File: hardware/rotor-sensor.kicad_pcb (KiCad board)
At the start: 2 copper layers, 30.7 x 16 mm, 33 parts, among them J1 Conn_01x03, J2 Conn_01x03, J3 Conn_01x03, U1 ATtiny202-SS, U2 EE-SX199, U3 SM351LT

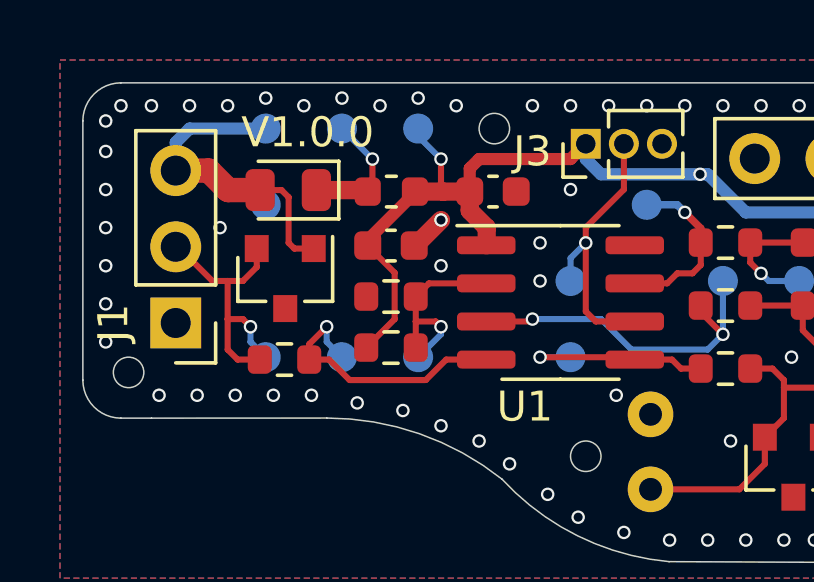
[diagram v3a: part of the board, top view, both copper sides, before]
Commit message: Rotated input filter capacitor for better ground connection
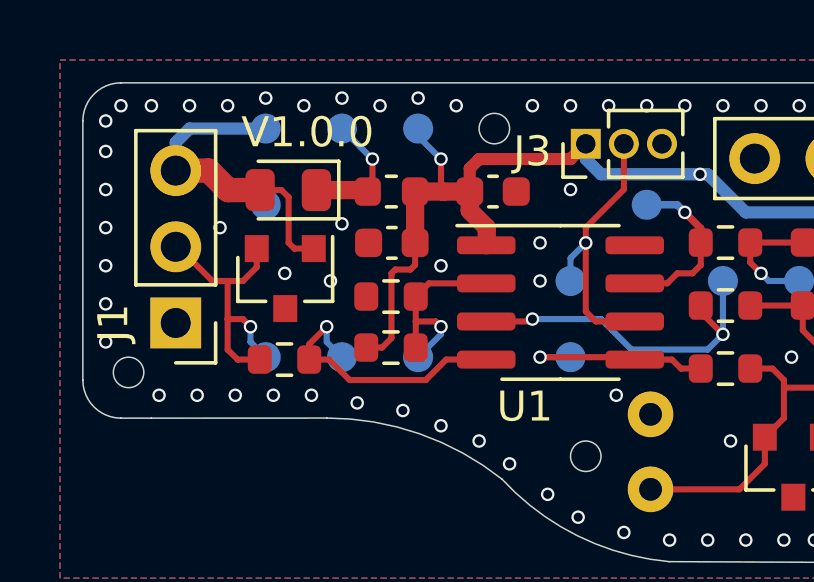
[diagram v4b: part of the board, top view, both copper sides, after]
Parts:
- moved C1 0.09 mm to (-7.90, -3.89), turned to 180 degrees
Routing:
- net GND: track 1.24 -> 0.00 mm, vias 76 -> 78
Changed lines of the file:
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@@
     (thickness 1.6)
     (drawings 17)
-    (tracks 255)
+    (tracks 258)
     (zones 0)
     (modules 33)
@@
   )
   (setup
-    (last_trace_width 0.4064)
+    (last_trace_width 0.2032)
     (user_trace_width 0.2032)
     (user_trace_width 0.4064)
@@
   )
   (module Capacitor_SMD:C_0603_1608Metric (layer F.Cu)
-    (at -7.925 -3.8)
+    (at -7.896 -3.89 180)
     (descr "Capacitor SMD 0603 (1608 Metric), square (rectangular) end terminal, IPC_7351 nominal, (Body size source: IPC-SM-782 page 76, https://www.pcb-3d.com/wordpress/wp-content/uploads/ipc-sm-782a_amendment_1_and_2.pdf), generated with kicad-footprint-generator")
     (tags capacitor)
@@
       (effects (font (size 0.4 0.4) (thickness 0.06)))
     )
-    (pad 2 smd roundrect (at 0.775 0) (size 0.9 0.95) (layers F.Cu F.Paste F.Mask) (roundrect_rratio 0.25)
-      (net 1 GND))
-    (pad 1 smd roundrect (at -0.775 0) (size 0.9 0.95) (layers F.Cu F.Paste F.Mask) (roundrect_rratio 0.25)
+    (pad 2 smd roundrect (at 0.775 0 180) (size 0.9 0.95) (layers F.Cu F.Paste F.Mask) (roundrect_rratio 0.25)
+      (net 1 GND))
+    (pad 1 smd roundrect (at -0.775 0 180) (size 0.9 0.95) (layers F.Cu F.Paste F.Mask) (roundrect_rratio 0.25)
       (net 2 +5V))
     (model ${KISYS3DMOD}/Capacitor_SMD.3dshapes/C_0603_1608Metric.wrl
@@
   (gr_arc (start -16.926 0.682) (end -18.196 0.682) (angle -90) (layer Edge.Cuts) (width 0.05))
   (gr_line (start -10.068 1.948568) (end -15.91 1.952) (layer Edge.Cuts) (width 0.05))
-  (via (at -6.258 -4.652) (size 0.45) (drill 0.3) (layers F.Cu B.Cu) (net 1))
   (via (at -6.258 -3.128) (size 0.45) (drill 0.3) (layers F.Cu B.Cu) (net 1))
   (via (at -2.956 -3.89) (size 0.45) (drill 0.3) (layers F.Cu B.Cu) (net 1))
@@
   (via (at 9.744 -0.08) (size 0.45) (drill 0.3) (layers F.Cu B.Cu) (net 1))
   (via (at 5.426 -0.08) (size 0.45) (drill 0.3) (layers F.Cu B.Cu) (net 1))
-  (segment (start -7.11 -3.8) (end -6.258 -4.652) (width 0.6096) (layer F.Cu) (net 1))
-  (segment (start -7.15 -3.8) (end -7.11 -3.8) (width 0.6096) (layer F.Cu) (net 1))
+  (segment (start -7.15 -3.8) (end -7.11 -3.8) (width 0.6096) (layer F.Cu) (net 2))
   (via (at 11.776 4.111) (size 0.45) (drill 0.3) (layers F.Cu B.Cu) (net 1))
   (via (at 11.649 5.254) (size 0.45) (drill 0.3) (layers F.Cu B.Cu) (net 1))
   (via (at 11.014 5.889) (size 0.45) (drill 0.3) (layers F.Cu B.Cu) (net 1))
   (via (at 6.188 6.016) (size 0.45) (drill 0.3) (layers F.Cu B.Cu) (net 1))
-  (segment (start -7.125 -5.6) (end -7.125 -5.563) (width 0.4064) (layer F.Cu) (net 2))
-  (segment (start -8.7 -3.988) (end -8.7 -3.8) (width 0.4064) (layer F.Cu) (net 2))
-  (segment (start -7.125 -5.563) (end -8.7 -3.988) (width 0.4064) (layer F.Cu) (net 2))
+  (via (at -9.56 -4.525) (size 0.45) (drill 0.3) (layers F.Cu B.Cu) (net 1))
+  (via (at -9.941 -2.62) (size 0.45) (drill 0.3) (layers F.Cu B.Cu) (net 1))
+  (via (at -11.465 -2.874) (size 0.45) (drill 0.3) (layers F.Cu B.Cu) (net 1))
   (via (at -6.258 -6.684) (size 0.45) (drill 0.3) (layers F.Cu B.Cu) (net 2))
   (segment (start -7.02 -7.446) (end -6.258 -6.684) (width 0.2032) (layer B.Cu) (net 2))
@@
   (segment (start -6.19 -5.6) (end -5.3 -5.6) (width 0.6096) (layer F.Cu) (net 2))
   (segment (start -7.125 -5.6) (end -6.19 -5.6) (width 0.6096) (layer F.Cu) (net 2))
-  (segment (start -7.80161 -1.34839) (end -8.75 -0.4) (width 0.2032) (layer F.Cu) (net 2))
-  (segment (start -7.80161 -2.89361) (end -7.80161 -1.34839) (width 0.2032) (layer F.Cu) (net 2))
-  (segment (start -8.7 -3.792) (end -7.80161 -2.89361) (width 0.2032) (layer F.Cu) (net 2))
-  (segment (start -8.7 -3.8) (end -8.7 -3.792) (width 0.2032) (layer F.Cu) (net 2))
   (segment (start -4.734 -3.826) (end -4.75 -3.81) (width 0.6096) (layer F.Cu) (net 2))
   (segment (start -4.734 -4.398) (end -4.734 -3.826) (width 0.6096) (layer F.Cu) (net 2))
@@
   (segment (start 7.204 0.936) (end 7.204 -0.588) (width 0.4064) (layer B.Cu) (net 2))
   (segment (start 6.442 1.698) (end 7.204 0.936) (width 0.4064) (layer B.Cu) (net 2))
+  (segment (start -7.121 -5.596) (end -7.125 -5.6) (width 0.6096) (layer F.Cu) (net 2))
+  (segment (start -7.121 -3.89) (end -7.121 -5.596) (width 0.6096) (layer F.Cu) (net 2))
+  (segment (start -7.121 -3.89) (end -7.121 -3.154) (width 0.2032) (layer F.Cu) (net 2))
+  (segment (start -7.121 -3.154) (end -7.274 -3.001) (width 0.2032) (layer F.Cu) (net 2))
+  (segment (start -7.274 -3.001) (end -7.782 -3.001) (width 0.2032) (layer F.Cu) (net 2))
+  (segment (start -7.782 -3.001) (end -7.909 -2.874) (width 0.2032) (layer F.Cu) (net 2))
+  (segment (start -7.909 -2.874) (end -7.909 -0.715) (width 0.2032) (layer F.Cu) (net 2))
+  (segment (start -8.224 -0.4) (end -8.75 -0.4) (width 0.2032) (layer F.Cu) (net 2))
+  (segment (start -7.909 -0.715) (end -8.224 -0.4) (width 0.2032) (layer F.Cu) (net 2))
   (segment (start -13.878 -2.62) (end -13.37 -2.62) (width 0.2032) (layer F.Cu) (net 3))
   (segment (start -15.018 -3.76) (end -13.878 -2.62) (width 0.2032) (layer F.Cu) (net 3))

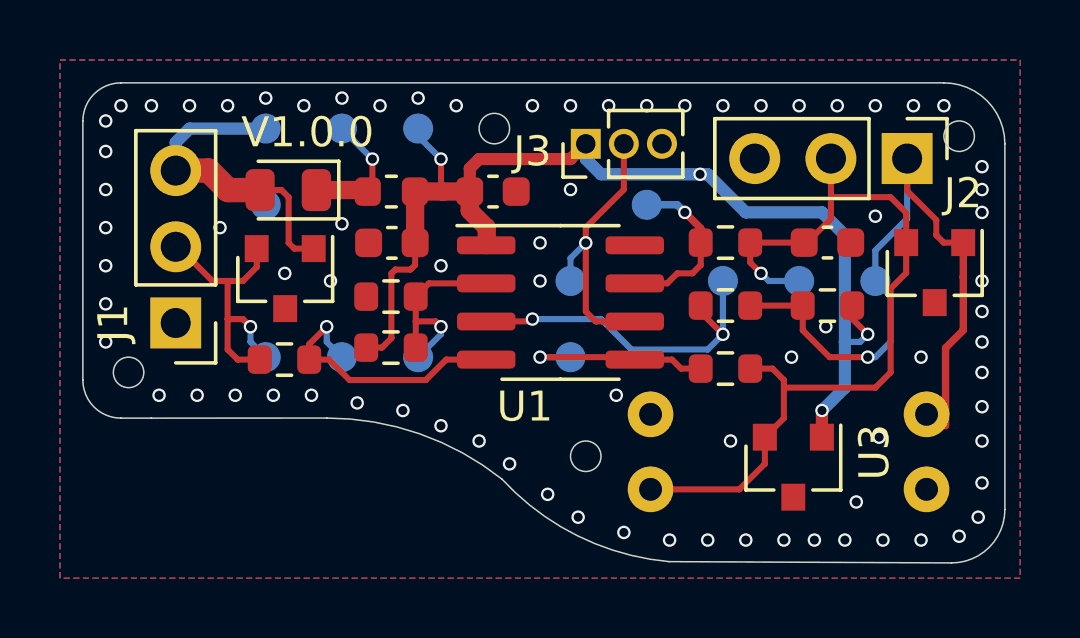
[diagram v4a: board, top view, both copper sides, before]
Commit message: Panelization workflow updates
Adds fiducials to board and added tab annotation as a footprint.
Panel configuration has been updated.
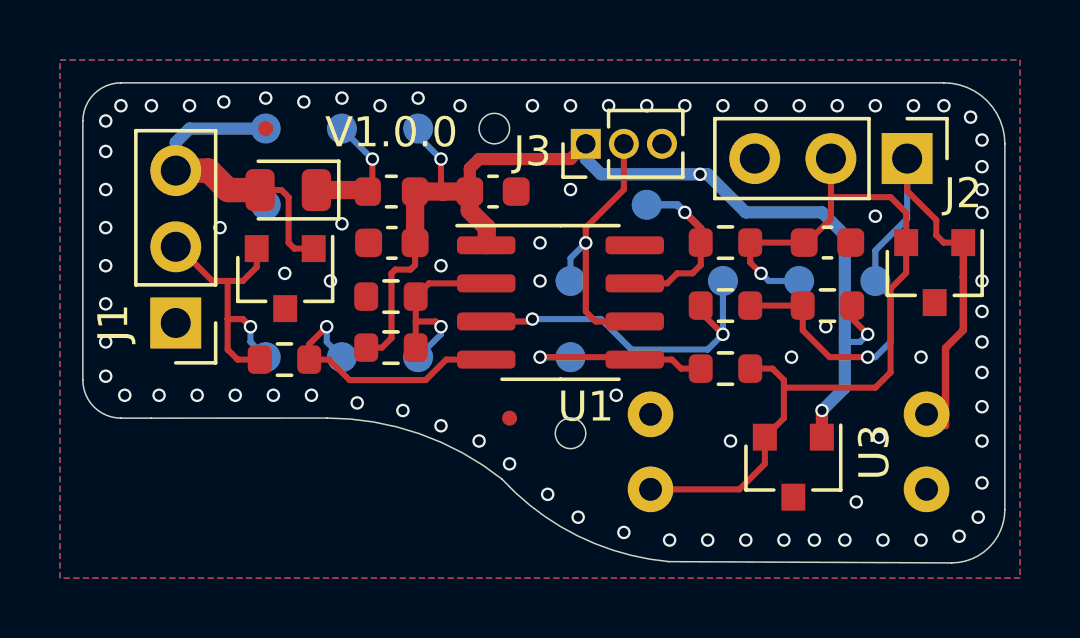
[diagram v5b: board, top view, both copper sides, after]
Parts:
- added FID1: Fiducial, Fiducial:Fiducial_0.5mm_Mask1.5mm, F.Cu at (-3.97, 1.95)
- added FID2: Fiducial, Fiducial:Fiducial_0.5mm_Mask1.5mm, F.Cu at (-12.1, -7.70)
- added REF**: Tab, local:Tab, F.Cu at (5.30, 7.29)
- added REF**: Tab, local:Tab, F.Cu at (-12.7, 2.59)
- added REF**: Tab, local:Tab, F.Cu at (6.70, -9.73)
- added REF**: Tab, local:Tab, F.Cu at (-8.93, -9.73)
- added REF**: Tab, local:Tab, F.Cu at (13.0, 1.32)
- added REF**: Tab, local:Tab, F.Cu at (-18.8, -3.38)
- C1, C2, C3: value C -> 100n
- L1: value L -> 10uH
- R1, R4, R5: value R -> 50m
- R2, R6, R7: value R -> 1k
- R3: value R -> 100
- TP2: value COM -> COMA
- TP7: value COM -> COMB
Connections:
- net Net-(D1-Pad1) renamed /Vin
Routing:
- net GND: vias 78 -> 82
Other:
- outline, holes or cut-outs redrawn

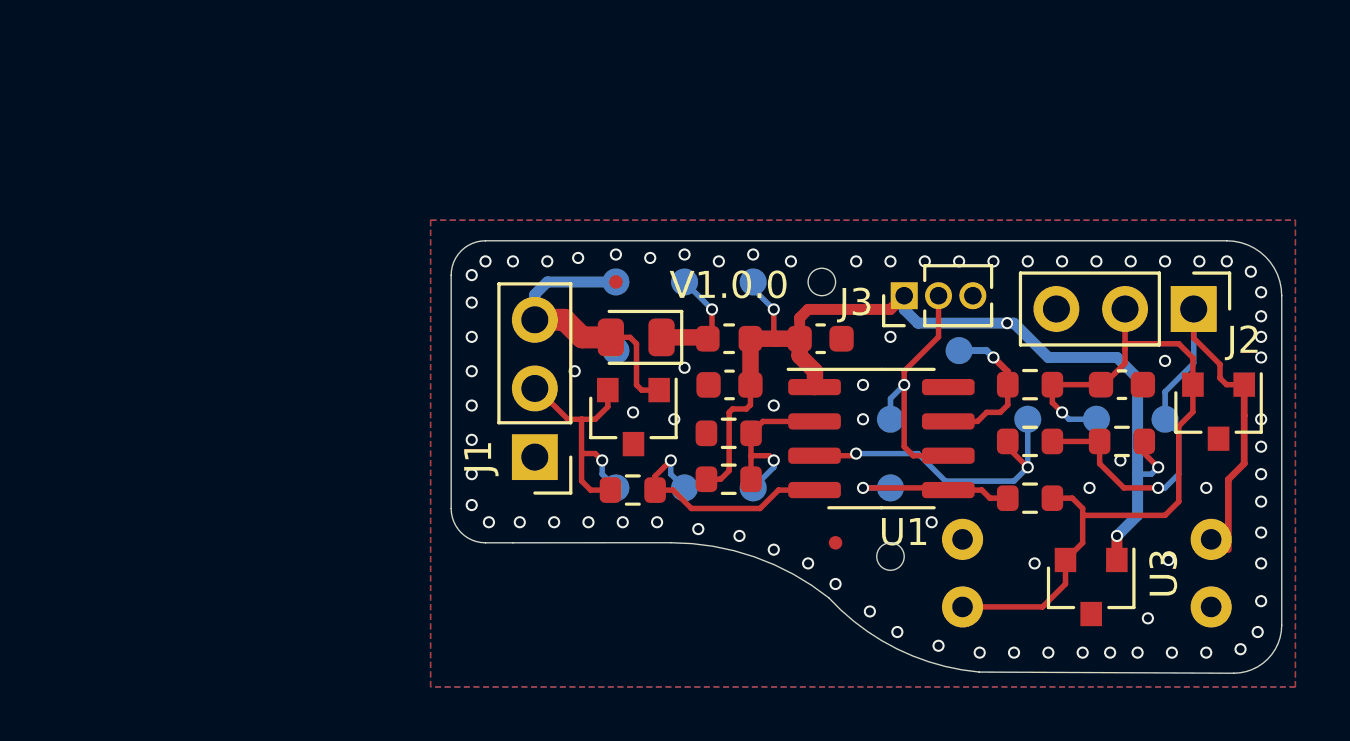
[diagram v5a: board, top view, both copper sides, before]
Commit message: Adds LIN Transceiver to the design (#7)
Updates layout and schematic, replaced test point labels on schematic
Adds overcurrent protection IC and removes sense line

Hardware container version downgrade, KiKit downgrade
Hardware workflow retention day set to 5 days and
STEP generation step is skipped due to errors

Fixes track clearance issue on panelized layout
Tight frame and 1x4 panel layout
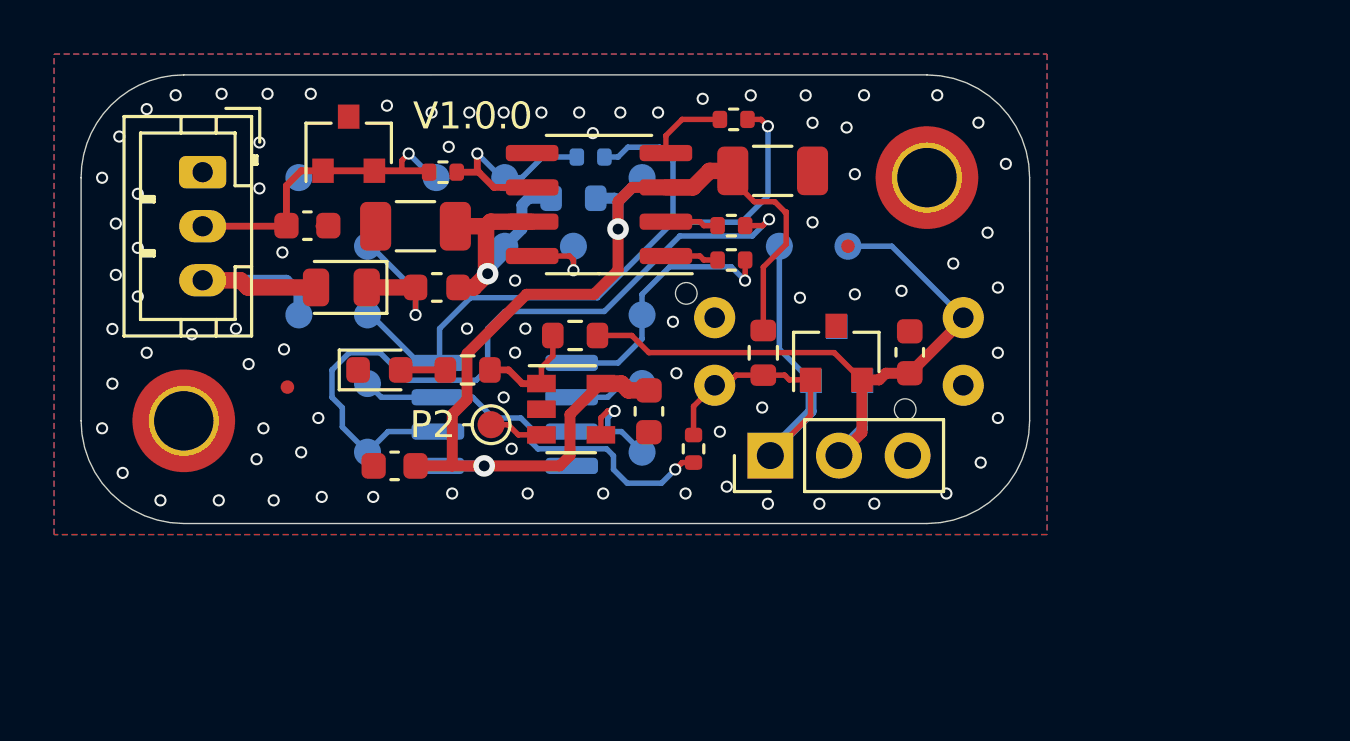
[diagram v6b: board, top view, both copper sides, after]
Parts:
- removed J3: Conn_01x03, Connector_PinHeader_1.27mm:PinHeader_1x03_P1.27mm_Vertical
- removed the R5 at (3.23, -1.80)
- removed the R6 at (-7.92, -0.40)
- removed REF** (x6): Tab, local:Tab
- added C2: 10u, Capacitor_SMD:C_1206_3216Metric, F.Cu at (-6.30, -11.8)
- added C3: 22p, Capacitor_SMD:C_0603_1608Metric, F.Cu at (-23.5, -9.78)
- added C5: 100n, Capacitor_SMD:C_0603_1608Metric, F.Cu at (-10.9, -2.91)
- added D4: LED_Small, LED_SMD:LED_0603_1608Metric, F.Cu at (-20.9, -4.45)
- added H1: MountingHole_Pad, MountingHole:MountingHole_2.2mm_M2_DIN965_Pad_TopOnly, F.Cu at (-28.1, -2.56)
- added H2: MountingHole_Pad, MountingHole:MountingHole_2.2mm_M2_DIN965_Pad_TopOnly, F.Cu at (-0.59, -11.6)
- added R1: 0, Resistor_SMD:R_0402_1005Metric, B.Cu at (-13.0, -12.3)
- added R10: 220, Resistor_SMD:R_0603_1608Metric, F.Cu at (-17.6, -4.45)
- added R2: 0, Resistor_SMD:R_0402_1005Metric, F.Cu at (-7.83, -8.51)
- added R3: 0, Resistor_SMD:R_0402_1005Metric, F.Cu at (-7.74, -13.7)
- added R9: 0, Resistor_SMD:R_0603_1608Metric, B.Cu at (-13.7, -10.8)
- added TP17: P2, TestPoint:TestPoint_Pad_D1.0mm, F.Cu at (-16.7, -2.42)
- added TP4: V3, TestPoint:TestPoint_Pad_D1.0mm, B.Cu at (-11.1, -11.6)
- added TP7: C1, TestPoint:TestPoint_Pad_D1.0mm, B.Cu at (-16.2, -11.6)
- added TP8: C2, TestPoint:TestPoint_Pad_D1.0mm, B.Cu at (-13.7, -9.02)
- added U2: MCP2021A-xxxxSN, Package_SO:SOIC-8_3.9x4.9mm_P1.27mm, F.Cu at (-12.7, -10.6)
- added U5: AP22804AW5, Package_TO_SOT_SMD:SOT-23-5, F.Cu at (-13.8, -2.99)
- C1: value 100n -> 10u; footprint Capacitor_SMD:C_0603_1608Metric -> Capacitor_SMD:C_1206_3216Metric
- J1: footprint Connector_PinHeader_2.54mm:PinHeader_1x03_P2.54mm_Vertical -> Connector_JST:JST_PH_B3B-PH-K_1x03_P2.00mm_Vertical
- R4: value 50m -> 0; footprint Resistor_SMD:R_0603_1608Metric -> Resistor_SMD:R_0402_1005Metric
- R5: renamed from R1; value 50m -> 0; footprint Resistor_SMD:R_0603_1608Metric -> Resistor_SMD:R_0402_1005Metric
- R7: value 1k -> 0; footprint Resistor_SMD:R_0603_1608Metric -> Resistor_SMD:R_0402_1005Metric
- TP1: value + -> V0
- TP10: renamed from TP7; value COMB -> M1
- TP11: renamed from TP8; value W2 -> M2
- TP12: renamed from TP9; value SENSE -> M3
- TP13: renamed from TP10; value AC- -> M6
- TP14: renamed from TP12; value IN -> P0
- TP15: renamed from TP11; value AC+ -> M7
- TP16: renamed from TP13; value OUT -> P1
- TP2: value COMA -> V1
- TP3: renamed from TP4; value VCC -> V2
- TP5: value - -> V4
- TP6: renamed from TP3; value VD -> C0
- TP9: renamed from TP6; value UPDI -> M0
- U3: moved to B.Cu
- U4: renamed from U1; moved to B.Cu
- moved TP15 24.5 mm to (-21.3, -3.94)
- moved FID2 21.1 mm to (-24.3, -3.81)
- moved R8 17.9 mm to (-13.6, -5.72)
- moved J2 16.6 mm to (-6.39, -1.27), turned to 90 degrees
- moved C4 16.5 mm to (-20.3, -0.89), turned to 180 degrees
- moved J1 16.2 mm to (-27.4, -11.8), turned to 270 degrees
- moved TP14 15.6 mm to (-6.05, -9.02)
- moved D2 14.6 mm to (-22.0, -12.8), turned to 90 degrees
- moved TP13 14.3 mm to (-21.3, -1.40)
- moved D3 14.3 mm to (-3.95, -5.08), turned to 90 degrees
- moved U4 14.0 mm to (-16.2, -2.80)
- moved R5 13.7 mm to (-18.5, -11.8)
- moved R6 13.7 mm to (-6.65, -5.08), turned to 90 degrees
- moved TP10 13.4 mm to (-21.3, -6.48)
- moved TP5 13.4 mm to (-23.8, -11.6)
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- renumbered C2 to C4, C3 to C6, D2 to D1, D1 to D2, FID2 to FID1, FID1 to FID2, R2 to R6, R3 to R8, U2 to U1
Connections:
- C1 pad 1: +5V -> /VIN_FILT
- D1 pad 1: Net-(D2-Pad1) -> Net-(D1-Pad1)
- D1 pad 2: /Vin -> /VIN
- D2 pad 1: /Vin -> /LIN_IN
- D2 pad 2: Net-(D1-Pad2) -> /LIN_IN
- J1 pad 2: Net-(D1-Pad2) -> /LIN_IN
- J1 pad 3: /Vin -> /VIN
- L1 pad 1: Net-(D2-Pad1) -> Net-(D1-Pad1)
- L1 pad 2: +5V -> /VIN_FILT
- R4 pad 1: PA3_ADC0_AIN3 -> PA6_GPIO
- R4 pad 2: /OS_OUTPUT -> Net-(R4-Pad2)
- R5 pad 1: PA1_USART0_TXD -> /LIN_BUS
- R5 pad 2: Net-(D1-Pad2) -> /LIN_IN
- R7 pad 1: PA6_AC0_AINN0 -> /OS_INPUT
- R7 pad 2: GND -> PA7_AC0_AINP0
- R8 pad 1: PA2_TCA2_W2 -> Net-(R10-Pad2)
- TP1 pad 1: /Vin -> /VIN
- TP11 pad 1: PA2_TCA2_W2 -> PA2_USART0_RXD
- TP12 pad 1: PA3_ADC0_AIN3 -> PA3_TCA0_W0
- TP13 pad 1: PA6_AC0_AINN0 -> PA6_GPIO
- TP2 pad 1: Net-(D1-Pad2) -> Net-(D1-Pad1)
- TP3 pad 1: +5V -> /VIN_FILT
- TP6 pad 1: Net-(D2-Pad1) -> /LIN_IN
- U3 pad 1: +5V -> /OS_OUTPUT
- U3 pad 2: /OS_OUTPUT -> /OS_INPUT
- U4 pad 2: PA6_AC0_AINN0 -> PA6_GPIO
- U4 pad 5: PA2_TCA2_W2 -> PA2_USART0_RXD
- U4 pad 7: PA3_ADC0_AIN3 -> PA3_TCA0_W0
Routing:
- net PA6_GPIO: track 0.00 -> 27.7 mm, vias 0 -> 1
- net PA1_USART0_TXD: track 9.03 -> 27.4 mm
- net /LIN_IN: track 0.00 -> 12.2 mm, vias 0 -> 1
- net /Vin: track 10.8 -> 0.00 mm
- net /VIN_FILT: track 0.00 -> 10.2 mm, vias 0 -> 1
- net PA2_USART0_RXD: track 0.00 -> 9.83 mm, vias 0 -> 1
- net Net-(D1-Pad2): track 9.57 -> 0.00 mm, vias 1 -> 0
- net /VIN: track 0.00 -> 8.87 mm
- net /LIN_BUS: track 0.00 -> 8.10 mm, vias 0 -> 1
- net PA0_UPDI: track 9.36 -> 2.82 mm, vias 1 -> 0
- net PA2_TCA2_W2: track 6.53 -> 0.00 mm, vias 1 -> 0
- net PA6_AC0_AINN0: track 6.48 -> 0.00 mm, vias 1 -> 0
- net Net-(D1-Pad1): track 0.00 -> 6.17 mm, vias 0 -> 1
- net PA3_ADC0_AIN3: track 5.80 -> 0.00 mm, vias 1 -> 0
- net /OS_INPUT: track 23.2 -> 18.1 mm, vias 1 -> 0
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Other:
- board size 30.7 x 16 mm -> 35.1 x 16.6 mm
